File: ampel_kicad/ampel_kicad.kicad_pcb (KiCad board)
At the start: 2 copper layers, 81.8 x 58.4 mm, 21 parts, among them J1 Power, J2 Digital/PWM, J3 Analog, J4 Digital/PWM, J5 Conn_Extern, J6 Conn_Main, SW1 SW_Push

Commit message: check
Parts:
- R4 10k: renamed from R4
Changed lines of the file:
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@@
 			(layer "F.Fab")
 		)
-		(fp_text user "C1 0,1µ"
+		(fp_text user "C1"
 			(at 3.75 0 90)
 			(layer "F.SilkS")
@@
 		(descr "Resistor, Axial_DIN0207 series, Axial, Horizontal, pin pitch=7.62mm, 0.25W = 1/4W, length*diameter=6.3*2.5mm^2, http://cdn-reichelt.de/documents/datenblatt/B400/1_4W%23YAG.pdf")
 		(tags "Resistor Axial_DIN0207 series Axial Horizontal pin pitch 7.62mm 0.25W = 1/4W length 6.3mm diameter 2.5mm")
-		(property "Reference" "R4"
+		(property "Reference" "R4 10k"
 			(at 3.81 0 90)
 			(layer "F.SilkS")

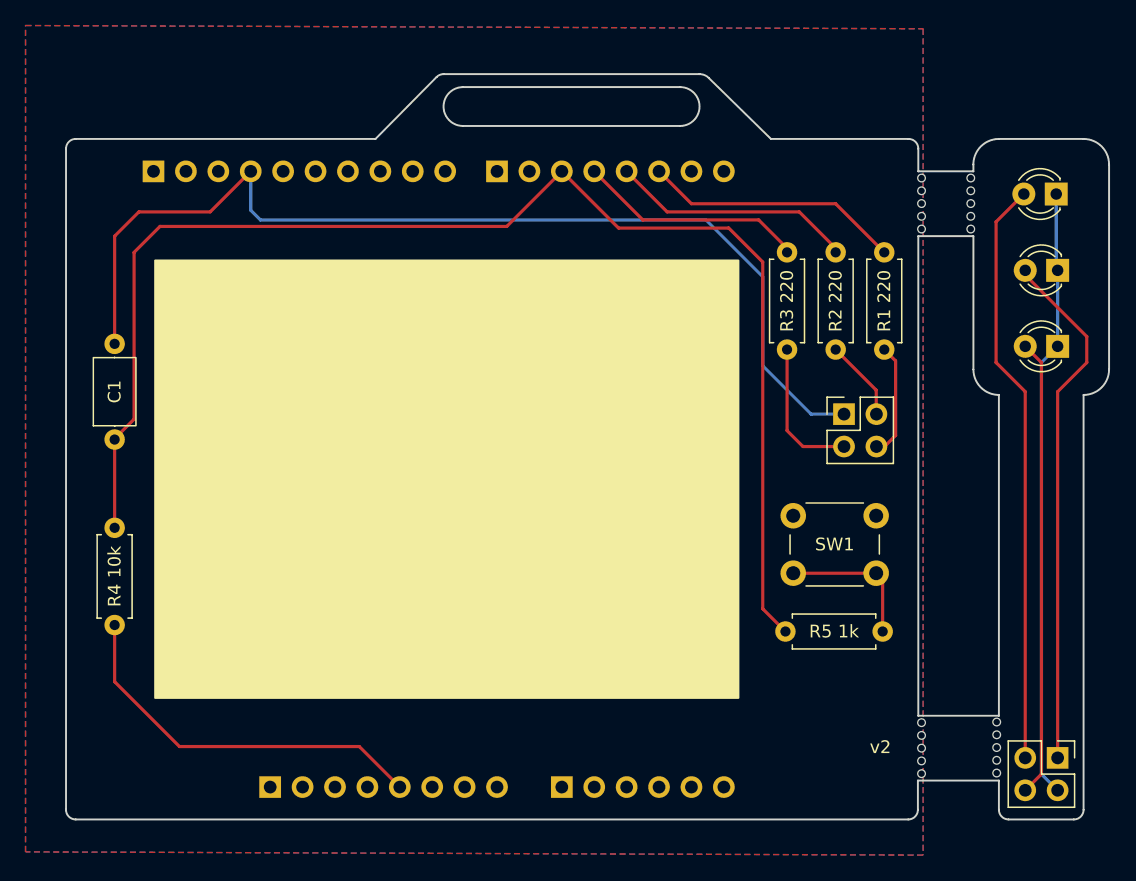
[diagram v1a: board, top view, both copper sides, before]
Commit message: update: no debounce
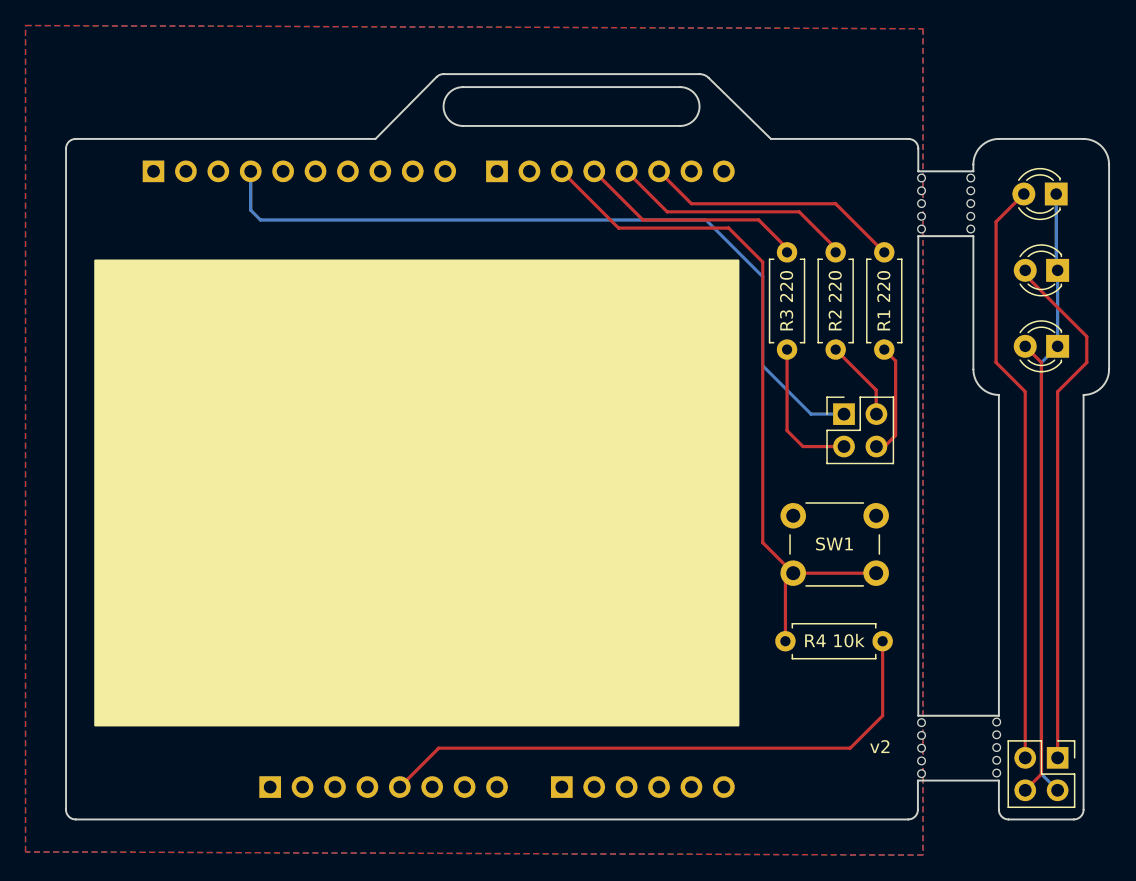
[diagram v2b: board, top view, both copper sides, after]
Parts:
- removed C1: 0,1 µF, Capacitor_THT:C_Axial_L5.1mm_D3.1mm_P7.50mm_Horizontal
- removed R5: 1 kOhm, Resistor_THT:R_Axial_DIN0207_L6.3mm_D2.5mm_P7.62mm_Horizontal
- moved R4 10k 53.3 mm to (156.4, 86.0), turned to 0 degrees
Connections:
- SW1 pad 2: Net-(R5-Pad2) -> /*5
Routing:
- net /*5: track 106.8 -> 57.7 mm
- net GND: track 80.6 -> 59.5 mm
- net +5V: track 30.2 -> 46.0 mm
- net Net-(R5-Pad2): track 12.9 -> 0.00 mm
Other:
- board text added: "https://ddi.ifi.lmu.de/tdi/2026/"

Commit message: JLC-Badge_Number + Date
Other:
- board text added: "07-2026"
- board text added: "JLCJLCJLCJLC"
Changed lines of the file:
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@@
 			(layer "F.Fab")
 		)
-		(fp_text user "${REFERENCE}"
+		(fp_text user "SW"
 			(at 3.25 2.25 0)
 			(layer "F.SilkS")
@@
 				(font
 					(size 1 1)
-					(thickness 0.1)
+					(thickness 0.15)
 				)
 				(justify left bottom mirror)
@@
 		)
 	)
+	(gr_text "07-2026"
+		(at 112.192 97.46 -0)
+		(layer "B.SilkS")
+		(effects
+			(font
+				(size 1 1)
+				(thickness 0.15)
+			)
+			(justify left bottom mirror)
+		)
+	)
 	(gr_text "https://ddi.ifi.lmu.de/tdi/2026/"
 		(at 175.438 66.726 90)
@@
 			(font
 				(size 1 1)
-				(thickness 0.1)
+				(thickness 0.15)
+			)
+			(justify left bottom mirror)
+		)
+	)
+	(gr_text "JLCJLCJLCJLC"
+		(at 112.192 98.984 -0)
+		(layer "B.SilkS")
+		(effects
+			(font
+				(size 1 1)
+				(thickness 0.15)
 			)
 			(justify left bottom mirror)
